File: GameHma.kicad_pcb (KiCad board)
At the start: 2 copper layers, 14 parts, among them J2 Motor_Terminal_01x04, J3 Motor_Terminal_01x04, J4 Motor_Terminal_01x04, J5 Motor_Terminal_01x04, U1 ESP32-DEVKIT-V1, U2 A4988_STEPPER_MOTOR_DRIVER_CA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, U3 A4988_STEPPER_MOTOR_DRIVER_CA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, U4 A4988_STEPPER_MOTOR_DRIVER_CA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, U5 A4988_STEPPER_MOTOR_DRIVER_CA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, U6 SRT_MP1584EN

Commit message: Add log, Finish PCB rout line
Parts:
- added J1: Screw_Terminal_01x02, TerminalBlock_Phoenix:TerminalBlock_Phoenix_MKDS-1,5-2-5.08_1x02_P5.08mm_Horizontal, F.Cu at (130.2, 64.8)
- moved J3 114.8 mm to (182.8, 125.0), turned to 90 degrees
- moved J2 107.6 mm to (183.3, 94.7), turned to 90 degrees
- moved U3 92.7 mm to (172.5, 121.3), turned to 0 degrees
- moved U2 88.2 mm to (172.8, 90.7), turned to 0 degrees
- moved C4 76.3 mm to (103.2, 95.0)
- moved C3 69.1 mm to (114.2, 126.3), turned to 0 degrees
- moved J5 47.2 mm to (107.0, 74.0), turned to -90 degrees
- moved J4 45.5 mm to (107.2, 104.5), turned to -90 degrees
- moved U6 45.1 mm to (151.3, 69.4), turned to 0 degrees
- moved U1 34.2 mm to (146.6, 106.2), turned to 0 degrees
- moved U5 25.0 mm to (117.5, 77.3), turned to 180 degrees
- moved U4 23.7 mm to (117.5, 108.3), turned to 180 degrees
- moved C1 22.0 mm to (170.8, 73.0), turned to 0 degrees
- moved C2 16.8 mm to (187.6, 108.2)
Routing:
- net +V_{DD}: track 416.3 -> 250.0 mm
- net +V_{batt}: track 252.3 -> 392.9 mm
- net GND: track 375.4 -> 468.3 mm
- net DIR_3: track 94.1 -> 13.9 mm
- net STEP_4: track 18.9 -> 53.9 mm
- net DIR_4: track 9.12 -> 39.2 mm
- net STEP_3: track 38.9 -> 13.9 mm
- net STEP_1: track 10.8 -> 17.5 mm
- net DIR_1: track 10.8 -> 17.1 mm
- net STEP_2: track 8.82 -> 7.71 mm
- net DIR_2: track 8.82 -> 7.71 mm

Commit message: add 3d model
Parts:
- moved J1 5.18 mm to (135.4, 64.8), turned to 180 degrees
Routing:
- net +V_{DD}: track 250.0 -> 252.3 mm
- net DIR_4: track 39.2 -> 39.8 mm
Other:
- board outline added: 98 x 82 mm

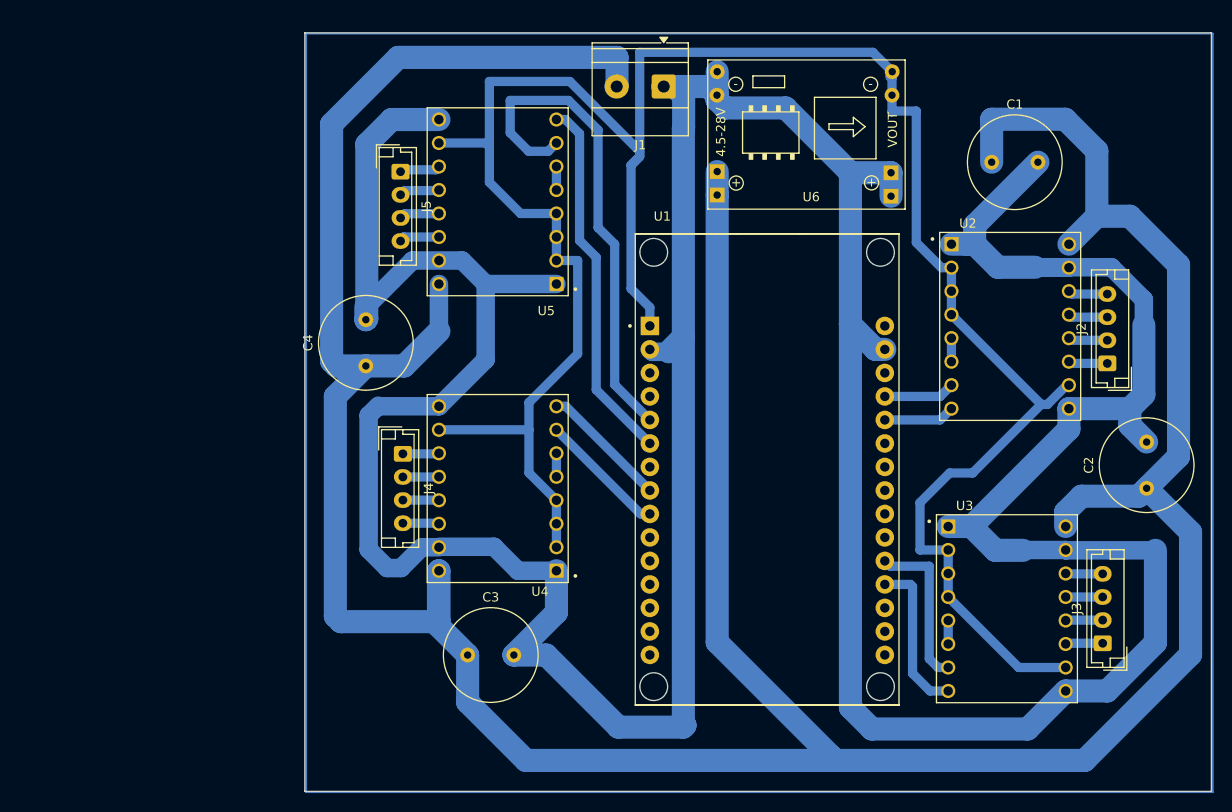
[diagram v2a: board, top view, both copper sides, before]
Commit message: Dril a hole M3
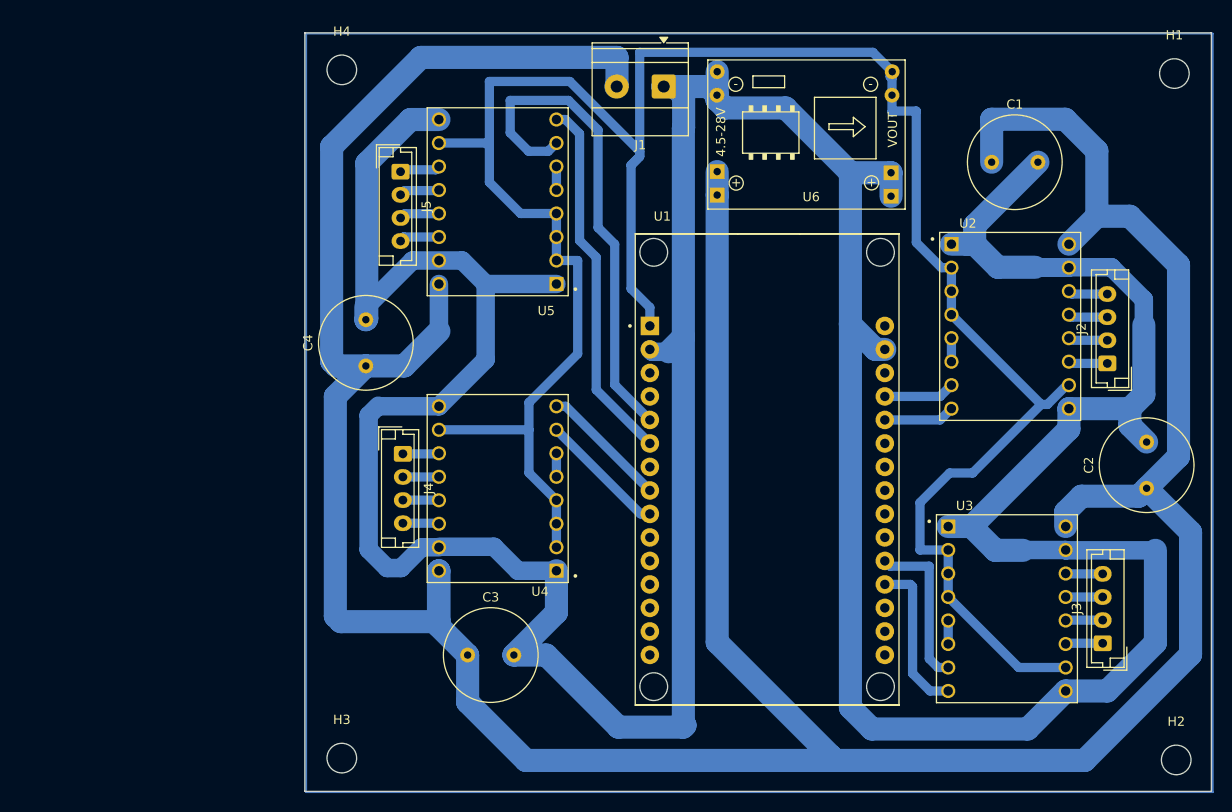
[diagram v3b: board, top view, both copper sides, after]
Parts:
- added H1: MountingHole, MountingHole:MountingHole_3.2mm_M3, F.Cu at (190.6, 63.4)
- added H2: MountingHole, MountingHole:MountingHole_3.2mm_M3, F.Cu at (190.8, 137.6)
- added H3: MountingHole, MountingHole:MountingHole_3.2mm_M3, F.Cu at (100.6, 137.4)
- added H4: MountingHole, MountingHole:MountingHole_3.2mm_M3, F.Cu at (100.6, 63.0)
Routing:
- net +V_{batt}: track 392.9 -> 391.5 mm
- net GND: track 468.3 -> 467.1 mm
